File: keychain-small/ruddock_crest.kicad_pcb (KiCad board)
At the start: 2 copper layers, 38 x 45.3 mm, 4 parts

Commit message: New hole design
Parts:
- moved REF** 0.13 mm to (141.0, 85.3)
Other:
- board size 38 x 45.3 mm -> 38.1 x 45.7 mm
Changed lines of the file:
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@@
   (general
     (thickness 1.6)
-    (drawings 22)
+    (drawings 28)
     (tracks 0)
     (zones 0)
@@
   (title_block
     (title "Ruddock House PCB Crest")
-    (date 2019-02-12)
+    (date 2019-02-13)
     (rev A)
     (company "Ruddock House Electrical Engineering")
@@
   )
   (module MountingHole:MountingHole_3.2mm_M3_DIN965_Pad (layer F.Cu)
-    (at 140.97 85.471)
+    (at 140.97 85.344)
     (descr "Mounting Hole 3.2mm, M3, DIN965")
     (tags "mounting hole 3.2mm m3 din965")
@@
       (xy 9.730745 -13.40817) (xy 9.745385 -13.421618) (xy 9.978417 -13.636419) (xy 10.013345 -13.51111)) (layer F.Mask) (width 0.01))
   )
-  (dimension 41.529 (width 0.3) (layer Dwgs.User)
-    (gr_text "41.529 mm" (at 166.946 106.2355 270) (layer Dwgs.User)
+  (gr_poly (pts (xy 144.78 89.408) (xy 141.478 88.9) (xy 143.51 87.884) (xy 144.78 86.106)) (layer B.SilkS) (width 0.15))
+  (gr_poly (pts (xy 144.78 89.408) (xy 141.478 88.9) (xy 143.51 87.884) (xy 144.78 86.106)) (layer F.SilkS) (width 0.15))
+  (gr_poly (pts (xy 137.16 89.408) (xy 140.208 88.9) (xy 138.684 88.138) (xy 137.16 86.106)) (layer B.SilkS) (width 0.15))
+  (gr_poly (pts (xy 137.16 89.408) (xy 140.208 88.9) (xy 138.684 88.138) (xy 137.16 86.106)) (layer F.SilkS) (width 0.15))
+  (gr_line (start 137.16 85.344) (end 137.16 89.408) (layer B.SilkS) (width 0.57))
+  (gr_line (start 144.78 85.344) (end 144.78 89.408) (layer B.SilkS) (width 0.57))
+  (gr_line (start 144.78 85.344) (end 144.78 89.408) (layer F.SilkS) (width 0.57))
+  (gr_arc (start 140.97 85.344) (end 144.78 85.344) (angle -180) (layer B.SilkS) (width 0.57))
+  (gr_circle (center 140.97 85.344) (end 144.47 85.344) (layer B.SilkS) (width 0.5))
+  (gr_line (start 137.16 85.344) (end 137.16 89.408) (layer F.SilkS) (width 0.57))
+  (gr_arc (start 140.97 85.344) (end 144.78 85.344) (angle -180) (layer F.SilkS) (width 0.57))
+  (gr_line (start 145.034 85.344) (end 145.034 89.3445) (layer Edge.Cuts) (width 0.1))
+  (gr_line (start 136.906 85.344) (end 136.906 89.3445) (layer Edge.Cuts) (width 0.1))
+  (gr_arc (start 140.97 107.95) (end 136.906001 89.344501) (angle -335.3568188) (layer Edge.Cuts) (width 0.1))
+  (gr_line (start 121.92 107.95) (end 160.02 107.95) (layer Dwgs.User) (width 0.1))
+  (gr_arc (start 140.97 85.344) (end 145.034 85.344) (angle -180) (layer Edge.Cuts) (width 0.1))
+  (gr_circle (center 140.97 85.344) (end 144.47 85.344) (layer F.SilkS) (width 0.5))
+  (gr_line (start 140.97 128.27) (end 140.97 78.74) (layer Dwgs.User) (width 0.1))
+  (dimension 38.1 (width 0.3) (layer Dwgs.User)
+    (gr_text "38.100 mm" (at 140.97 134.179999) (layer Dwgs.User)
       (effects (font (size 1.5 1.5) (thickness 0.3)))
     )
-    (feature1 (pts (xy 149.098 127) (xy 165.432421 127)))
-    (feature2 (pts (xy 149.098 85.471) (xy 165.432421 85.471)))
-    (crossbar (pts (xy 164.846 85.471) (xy 164.846 127)))
-    (arrow1a (pts (xy 164.846 127) (xy 164.259579 125.873496)))
-    (arrow1b (pts (xy 164.846 127) (xy 165.432421 125.873496)))
-    (arrow2a (pts (xy 164.846 85.471) (xy 164.259579 86.597504)))
-    (arrow2b (pts (xy 164.846 85.471) (xy 165.432421 86.597504)))
+    (feature1 (pts (xy 160.02 128.27) (xy 160.02 132.66642)))
+    (feature2 (pts (xy 121.92 128.27) (xy 121.92 132.66642)))
+    (crossbar (pts (xy 121.92 132.079999) (xy 160.02 132.079999)))
+    (arrow1a (pts (xy 160.02 132.079999) (xy 158.893496 132.66642)))
+    (arrow1b (pts (xy 160.02 132.079999) (xy 158.893496 131.493578)))
+    (arrow2a (pts (xy 121.92 132.079999) (xy 123.046504 132.66642)))
+    (arrow2b (pts (xy 121.92 132.079999) (xy 123.046504 131.493578)))
   )
-  (dimension 45.339044 (width 0.3) (layer Dwgs.User)
-    (gr_text "45.339 mm" (at 171.767588 104.290968 270.0802461) (layer Dwgs.User)
-      (effects (font (size 1.5 1.5) (thickness 0.3)))
-    )
-    (feature1 (pts (xy 143.5735 127) (xy 170.285761 126.962588)))
-    (feature2 (pts (xy 143.51 81.661) (xy 170.222261 81.623588)))
-    (crossbar (pts (xy 169.63584 81.624409) (xy 169.69934 126.963409)))
-    (arrow1a (pts (xy 169.69934 126.963409) (xy 169.111342 125.837728)))
-    (arrow1b (pts (xy 169.69934 126.963409) (xy 170.284182 125.836085)))
-    (arrow2a (pts (xy 169.63584 81.624409) (xy 169.050998 82.751733)))
-    (arrow2b (pts (xy 169.63584 81.624409) (xy 170.223838 82.75009)))
-  )
-  (gr_line (start 138.43 85.471) (end 143.51 85.471) (layer Dwgs.User) (width 0.1))
-  (gr_poly (pts (xy 148.082 90.424) (xy 141.986 88.9) (xy 144.272 87.376) (xy 144.526 84.328) (xy 143.256 82.296) (xy 146.558 84.328) (xy 148.082 87.63)) (layer B.SilkS) (width 0.15))
-  (gr_poly (pts (xy 148.082 90.424) (xy 141.986 88.9) (xy 144.272 87.376) (xy 144.526 84.328) (xy 143.256 82.296) (xy 146.558 84.328) (xy 148.082 87.63)) (layer F.SilkS) (width 0.15))
-  (gr_poly (pts (xy 133.858 90.424) (xy 139.954 88.9) (xy 137.668 87.376) (xy 137.414 84.328) (xy 138.938 82.042) (xy 135.128 84.582) (xy 133.858 87.63)) (layer B.SilkS) (width 0.15))
-  (gr_poly (pts (xy 133.858 90.424) (xy 139.954 88.9) (xy 137.668 87.376) (xy 137.414 84.328) (xy 138.938 82.042) (xy 135.128 84.582) (xy 133.858 87.63)) (layer F.SilkS) (width 0.15))
-  (gr_arc (start 140.97 89.145) (end 148.081999 90.437999) (angle -200.2) (layer B.SilkS) (width 0.5))
-  (gr_arc (start 140.97 89.145) (end 148.081999 90.437999) (angle -200.2) (layer F.SilkS) (width 0.5))
-  (gr_circle (center 140.97 85.471) (end 144.526 85.471) (layer B.SilkS) (width 0.5))
-  (gr_arc (start 140.97 89.14) (end 148.081999 90.423999) (angle -200.2) (layer F.SilkS) (width 0.5))
+  (gr_line (start 121.92 88.9) (end 121.92 127) (layer Dwgs.User) (width 0.1))
+  (gr_line (start 160.02 88.9) (end 121.92 88.9) (layer Dwgs.User) (width 0.1))
+  (gr_line (start 160.02 127) (end 160.02 88.9) (layer Dwgs.User) (width 0.1))
+  (gr_line (start 121.92 127) (end 160.02 127) (layer Dwgs.User) (width 0.1))
+  (gr_line (start 136.398 85.344) (end 145.542 85.344) (layer Dwgs.User) (width 0.1))
   (gr_line (start 140.716 89.154) (end 141.224 89.154) (layer Dwgs.User) (width 0.1))
-  (gr_line (start 140.97 78.74) (end 140.97 129.54) (layer Dwgs.User) (width 0.1))
-  (gr_arc (start 140.97 89.154) (end 148.335999 90.423999) (angle -199.5648141) (layer Edge.Cuts) (width 0.1))
-  (gr_line (start 149.352 90.424) (end 133.096 90.424) (layer Dwgs.User) (width 0.1))
-  (gr_arc (start 140.97 107.95) (end 133.604001 90.424001) (angle -314.4) (layer Edge.Cuts) (width 0.1))
-  (gr_circle (center 140.97 85.471) (end 144.526 85.471) (layer F.SilkS) (width 0.5))
   (gr_circle (center 140.97 107.95) (end 159.82 107.95) (layer B.SilkS) (width 0.5))
   (gr_circle (center 140.97 107.95) (end 159.82 107.95) (layer F.SilkS) (width 0.5))
-  (gr_circle (center 140.97 107.95) (end 139.7 107.95) (layer Dwgs.User) (width 0.1))
-  (dimension 38.1 (width 0.3) (layer Dwgs.User)
-    (gr_text "38.100 mm" (at 140.97 134.18) (layer Dwgs.User)
-      (effects (font (size 1.5 1.5) (thickness 0.3)))
-    )
-    (feature1 (pts (xy 160.02 111.76) (xy 160.02 132.666421)))
-    (feature2 (pts (xy 121.92 111.76) (xy 121.92 132.666421)))
-    (crossbar (pts (xy 121.92 132.08) (xy 160.02 132.08)))
-    (arrow1a (pts (xy 160.02 132.08) (xy 158.893496 132.666421)))
-    (arrow1b (pts (xy 160.02 132.08) (xy 158.893496 131.493579)))
-    (arrow2a (pts (xy 121.92 132.08) (xy 123.046504 132.666421)))
-    (arrow2b (pts (xy 121.92 132.08) (xy 123.046504 131.493579)))
-  )
   (gr_circle (center 140.97 107.95) (end 140.97 88.9) (layer Dwgs.User) (width 0.1))
 )

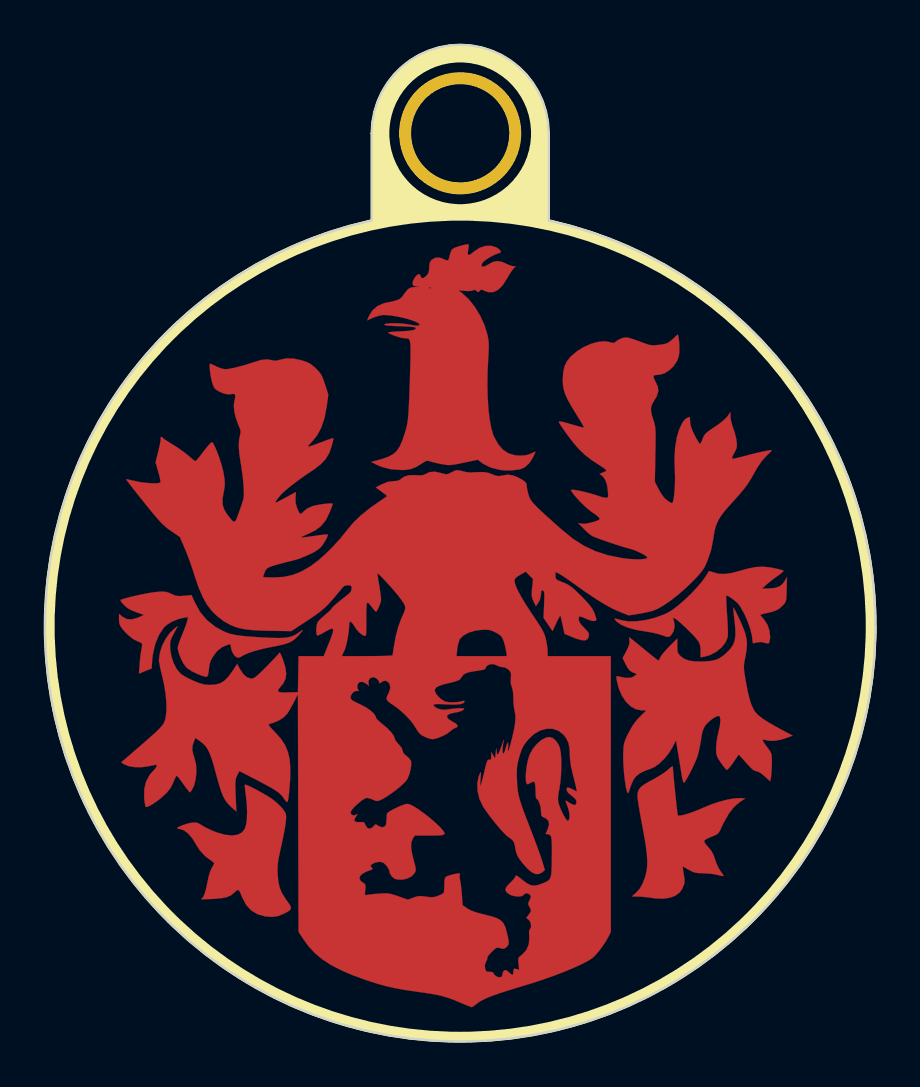
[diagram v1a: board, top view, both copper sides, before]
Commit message: Improve hole portrusion aesthetics
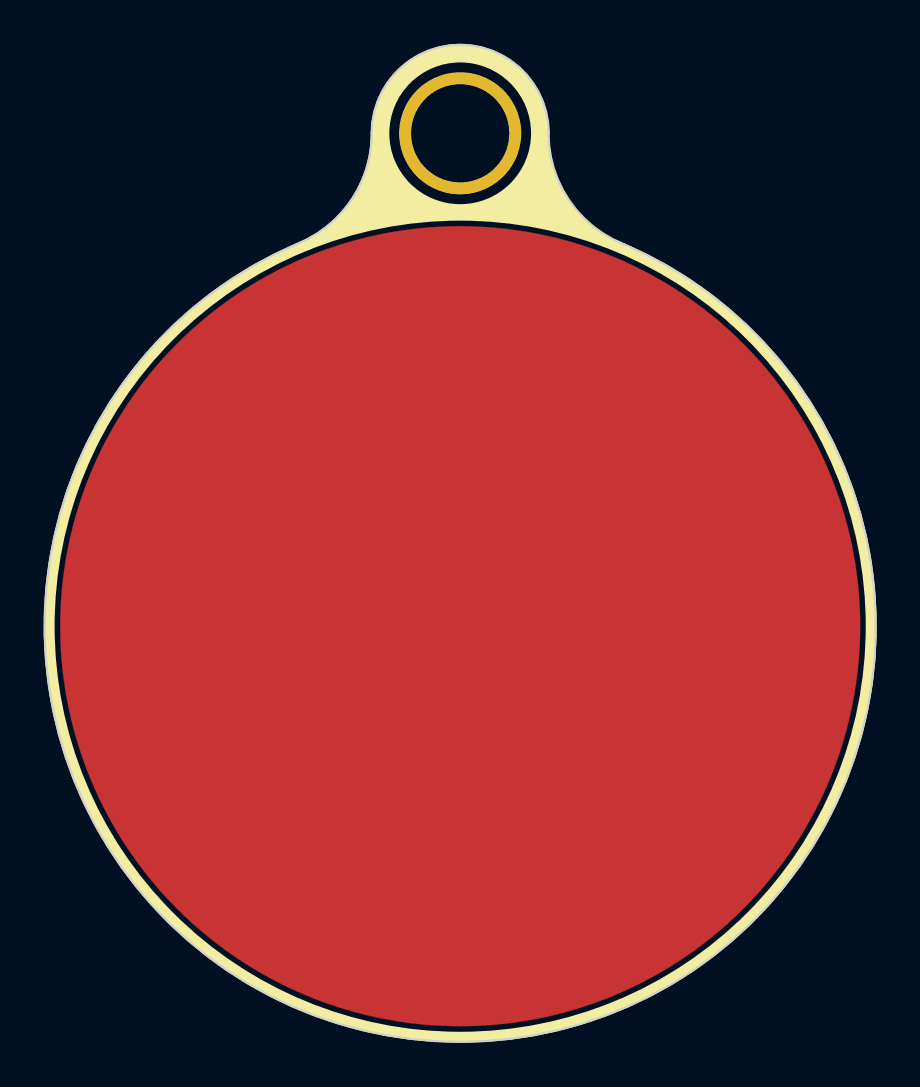
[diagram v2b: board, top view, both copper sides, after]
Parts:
- removed the G*** at (141.0, 108.2)
- added G***: LOGO, crest:circle_cu_1in5, F.Cu at (141.0, 108.0)
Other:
- outline, holes or cut-outs redrawn
- board text added: "GRID: 50 MIL"
